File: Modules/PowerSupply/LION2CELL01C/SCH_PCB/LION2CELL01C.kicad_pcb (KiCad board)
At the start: 2 copper layers, 80.8 x 60.5 mm, 97 parts, among them J1 JUMP_4X2, J10 JUMP_2x1, J11 JUMP_2x1, J12 JUMP_2x1, J13 JUMP_4X2, J14 JUMP_2x1, J2 JUMP_2x1, J3 JUMP_2x1, J4 JUMP_2x1, J5 JUMP_2x1, J6 JUMP_2x1, J7 JUMP_4X2, J8 CONN1_1, J9 CONN1_1, P1 _, P2 _, P3 _, P4 _, Q1 IRLML6244, Q2 MMBF170LT1G, Q3 MMBF170LT1G, Q4 BSS83P, SW1 SW_PUSH, U1 BQ29209, U2 BQ24103, U3 BQ34Z100, U4 SN74HC164D

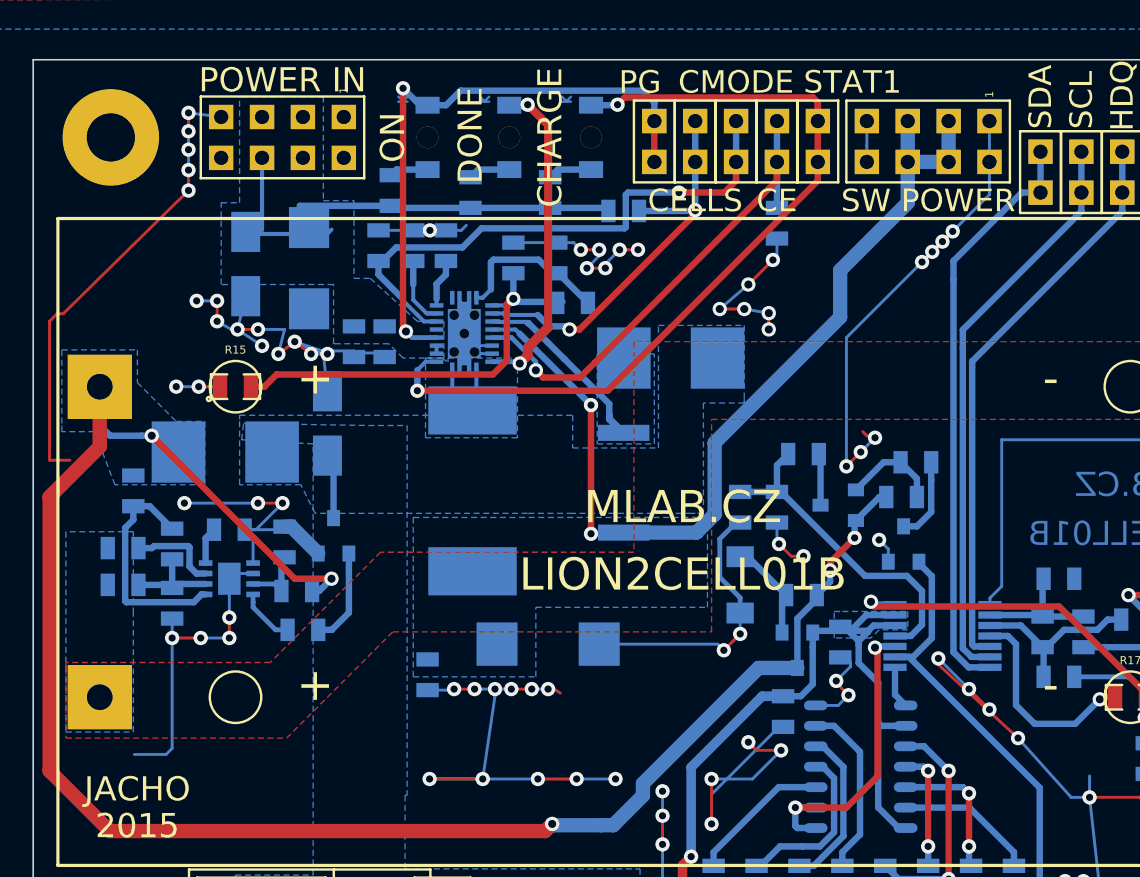
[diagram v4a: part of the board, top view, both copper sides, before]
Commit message: vycisteni spoju a nekterych prokovu.
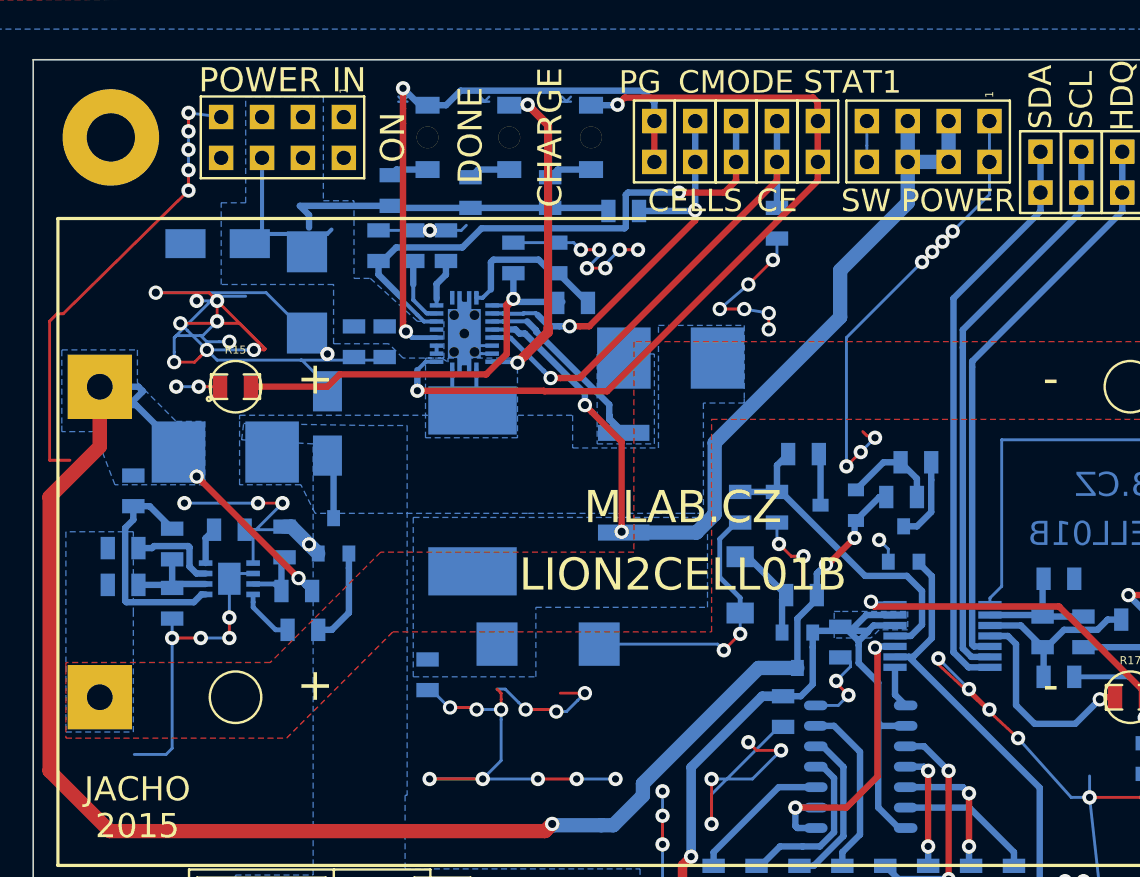
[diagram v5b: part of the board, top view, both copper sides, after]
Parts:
- moved D1 2.16 mm to (11.7, -49.3), turned to 0 degrees
- moved C2 1.51 mm to (17.3, -46.2)
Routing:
- net GND: track 406.8 -> 441.2 mm, vias 114 -> 112
- net (no net): track 0.00 -> 8.04 mm, vias 0 -> 3
- net /BAT+: track 115.9 -> 113.5 mm
- net Net-(C10-Pad1): track 56.7 -> 58.0 mm
- net /SDA: track 35.3 -> 34.6 mm

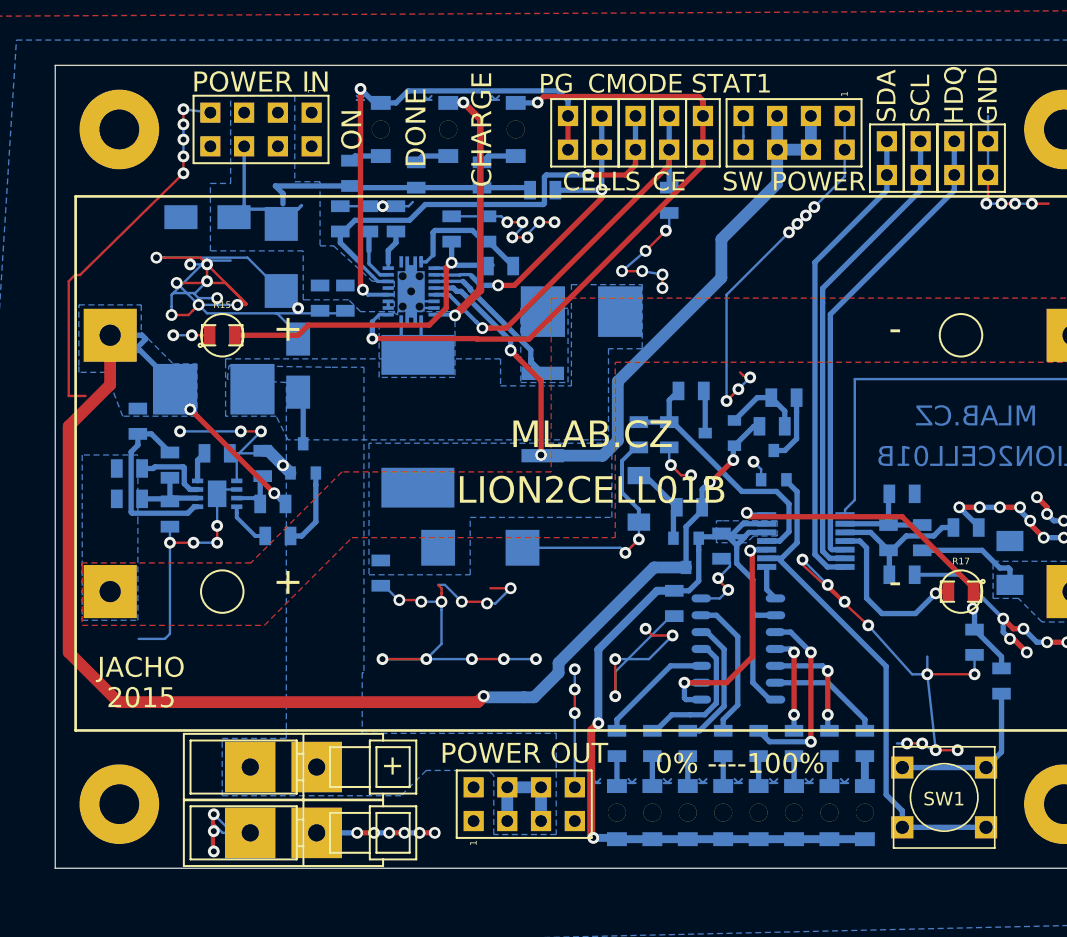
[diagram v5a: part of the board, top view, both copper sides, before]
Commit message: 
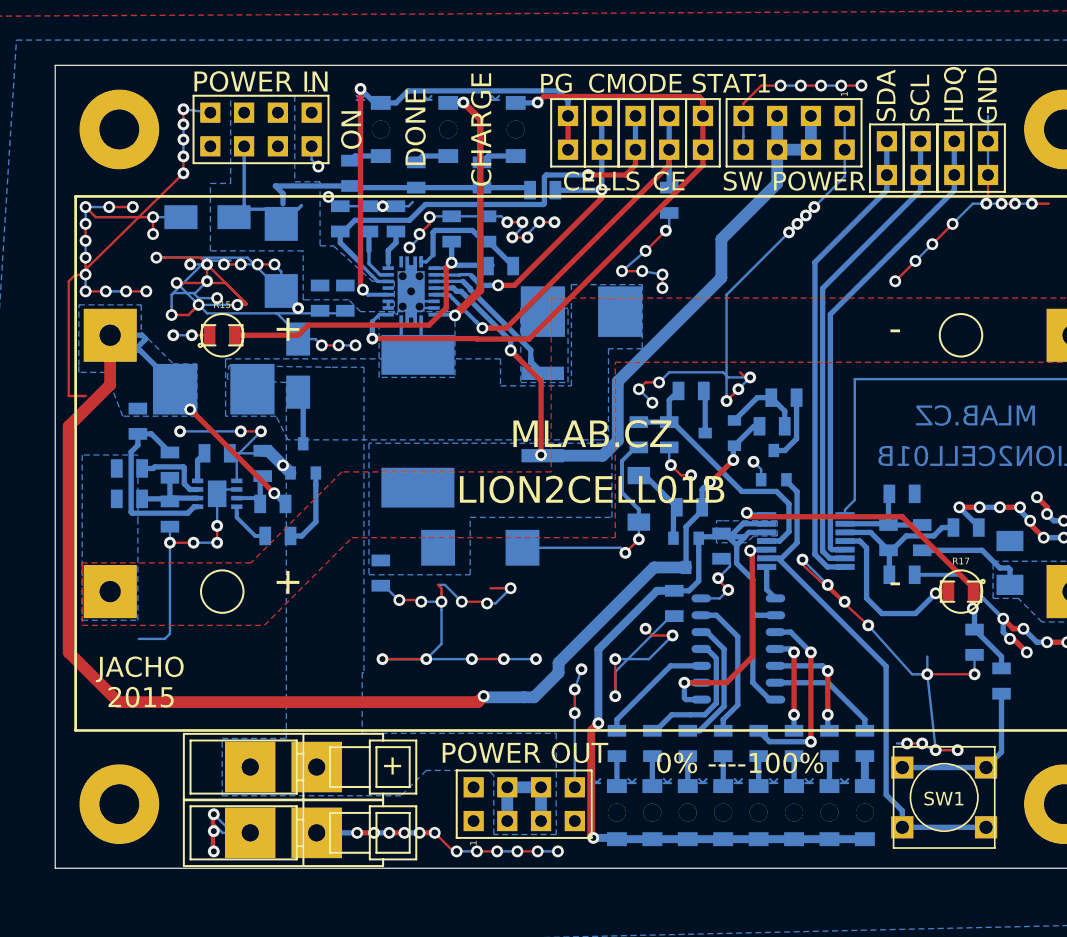
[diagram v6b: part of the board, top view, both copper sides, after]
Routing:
- net GND: track 441.2 -> 522.6 mm, vias 112 -> 155

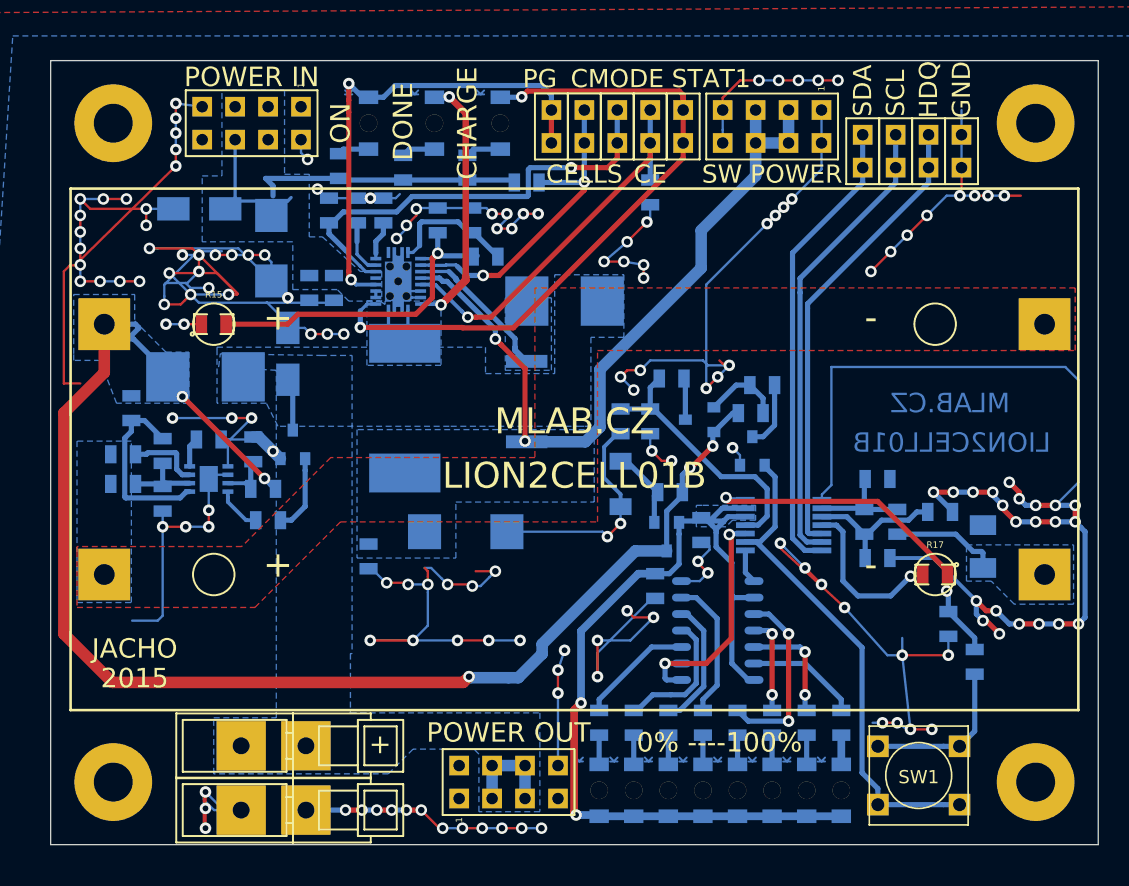
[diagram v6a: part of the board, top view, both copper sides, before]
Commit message: 
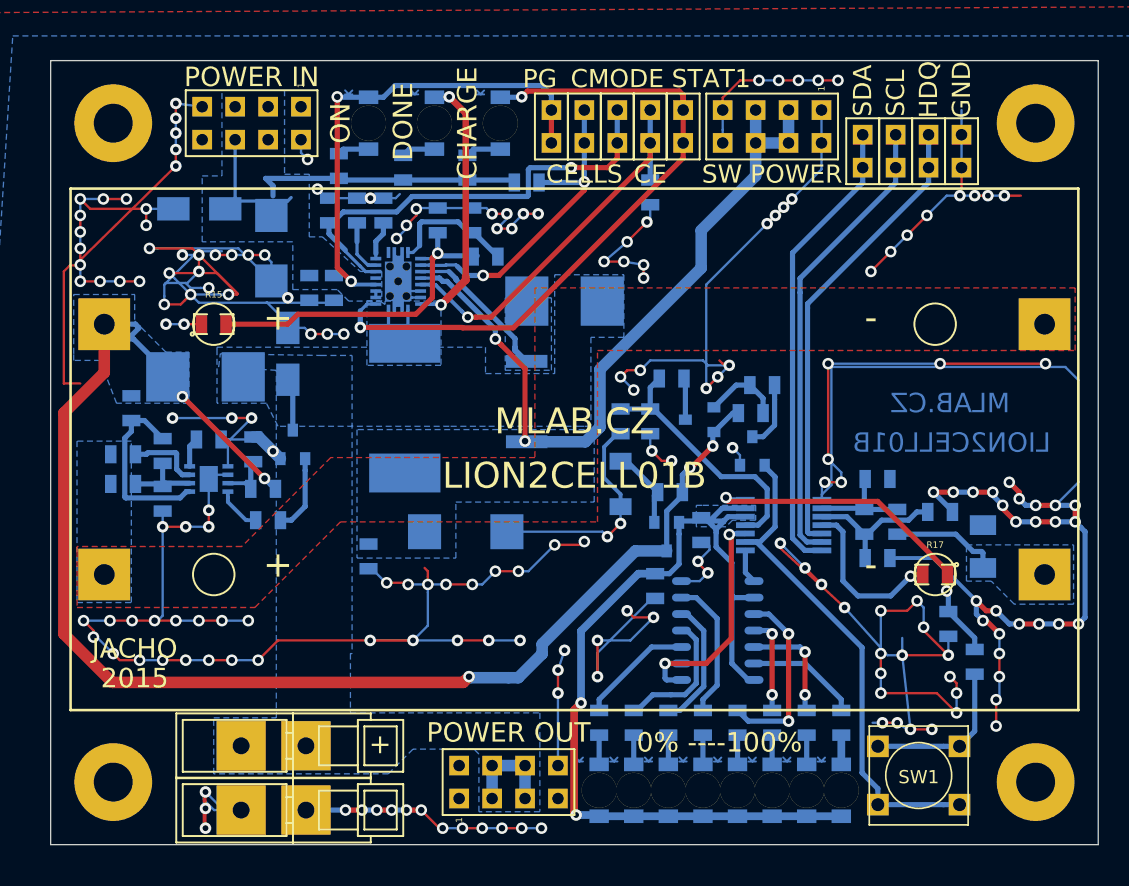
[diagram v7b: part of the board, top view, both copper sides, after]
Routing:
- net GND: track 522.6 -> 631.6 mm, vias 155 -> 196
- net (no net): track 8.04 -> 0.00 mm, vias 3 -> 0

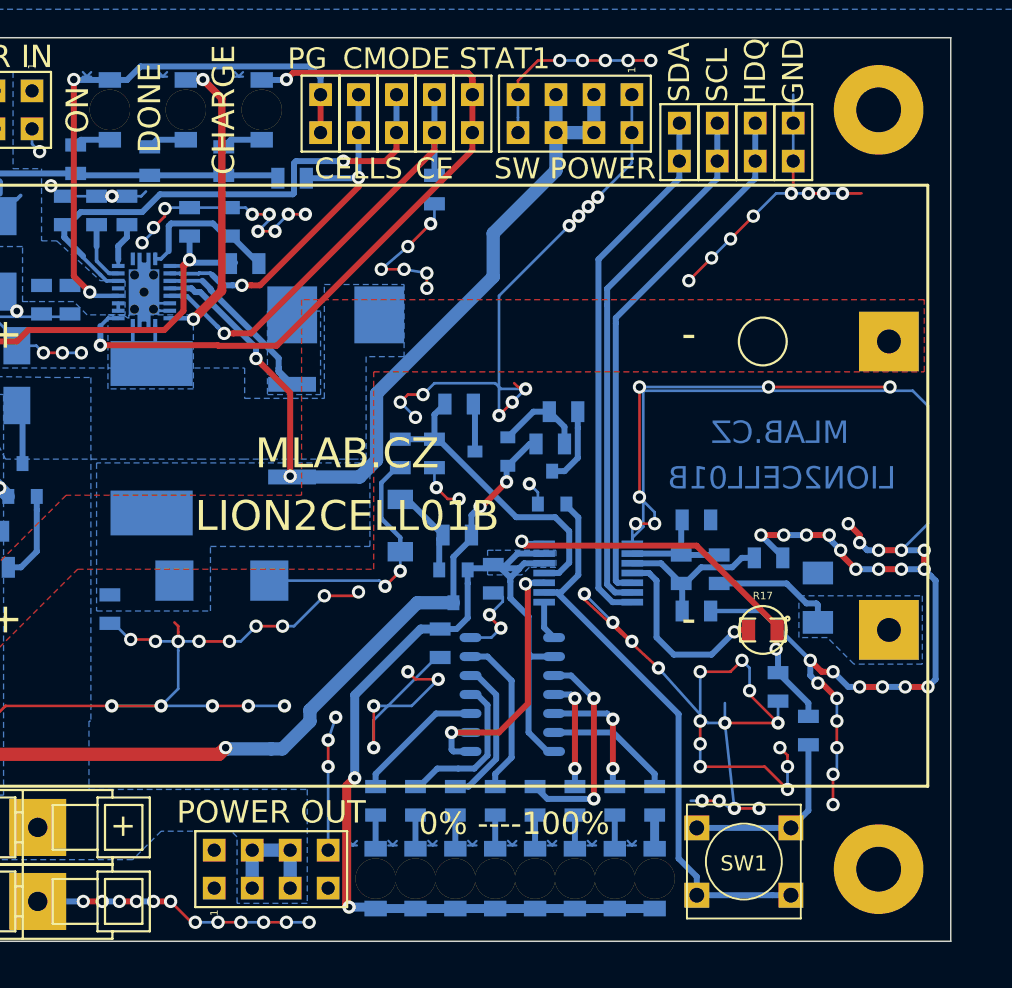
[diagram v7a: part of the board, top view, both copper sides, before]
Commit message: uprava modulu pred vyrobou
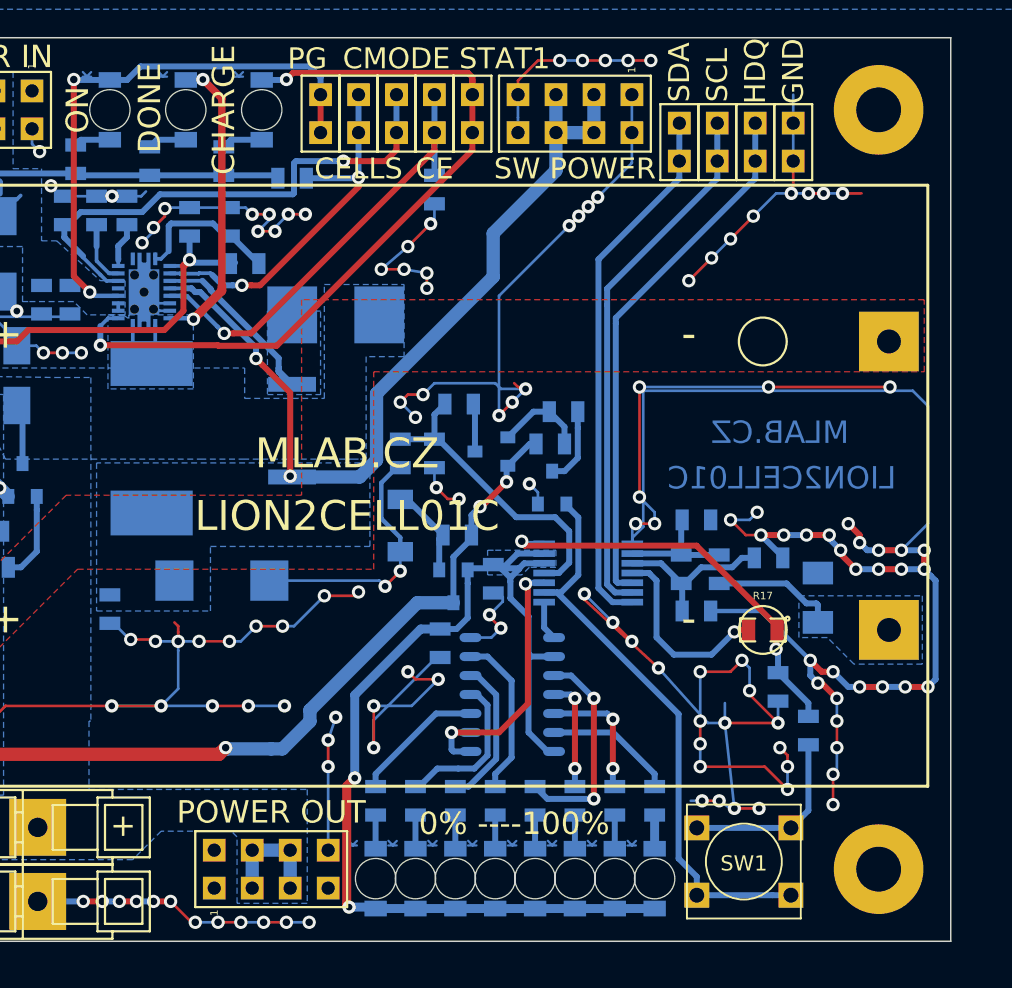
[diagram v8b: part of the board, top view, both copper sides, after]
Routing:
- net GND: track 631.6 -> 636.1 mm, vias 196 -> 198
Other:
- board text added: "LION2CELL01C"
- board text removed: "LION2CELL01B"
